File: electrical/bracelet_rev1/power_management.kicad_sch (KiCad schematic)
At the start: 16 parts, among them J1 USB_C_Receptacle_USB2.0_14P, Q1 PMOS, U3 MCP73831T-2ACI/OT, U4 XC6222B331MR-G

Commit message: Many schematic updates
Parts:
- added C25: 120pF, symbol Device:C
- added C26: 22uF, symbol Device:C
- added C27: 4.7uF, symbol Device:C
- added D3: D_Schottky, symbol Device:D_Schottky
- added L5: 1.0uH, symbol Device:L
- added Q2: PMOS, symbol Simulation_SPICE:PMOS
- added R10: 100k, symbol Device:R
- added R11: 499k, symbol Device:R
- added R12: 10k, symbol Device:R
- added R9: 200k, symbol Device:R
- added U6: TPS62A01DRL, Package_TO_SOT_SMD:SOT-563, symbol Regulator_Switching:TPS62A01DRL
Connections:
- net +BATT: now also Q2.1 (D)
- net GND: now also C26.2, C27.2, R10.2, R12.1, U6.1 (GND)
- net USB_VBUS: now also D3.2 (A), Q2.2 (G), R12.2
- net VDD renamed 3V3
- new net: C27.1, D3.1 (K), Q2.3 (S), R11.1, U6.3 (VIN), U6.4 (EN)
- new net: R11.2, U6.6 (PG)
- new net: L5.1, U6.2 (SW)
- new net: C25.2, R10.1, R9.2, U6.5 (FB)
- new net 1V8: C25.1, C26.1, L5.2, R9.1
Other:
- note added: "R1 = R2 x ((Vout/Vfb) - 1) = R2 x ((Vout/0.6V) - 1) => Select R2 as 100k (From datasheet) Sec 8.2"
- moved on the sheet: C16, C17, C18, C19, D1, D2, J1, Q1, R3, R4, R5, R6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

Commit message: Mostly finihsed hopefully but still needs clean up anyway
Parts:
- added J3: Conn_01x02, symbol Connector_Generic:Conn_01x02
- added R16: 200k, symbol Device:R
- added R17: 100k, symbol Device:R
- added R2: 100m, symbol Device:R_Shunt
- added U8: INA180A1, Package_TO_SOT_SMD:SOT-23-5, symbol Amplifier_Current:INA180A1
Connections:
- net +BATT: now also R16.1, R2.4
- net 3V3: now also U8.5 (V+)
- net GND: now also J3.2 (Pin_2), R17.2, U8.2 (GND)
- new net: J3.1 (Pin_1), R2.1
- new net: R2.2, U8.4 (-)
- new net: R2.3, U8.3 (+)
- new net CURR_SENSE: U8.1
- new net VBATT_SENSE: R16.2, R17.1
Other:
- moved on the sheet: C16, C17, C18, C19, C25, C26, C27, D1, D2, D3, J1, L5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

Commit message: May updates
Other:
- note added: "1V8 Buck"
- note added: "3V3 LDO"
- note added: "Battery Charging IC"
- note added: "Battery Current Sensing"
- note added: "Note: Not sure what Cin should be (C19)"
- note added: "USB-C Input"
- note removed: "Note: Maybe add reverse current protection here?"
- note removed: "Note: Not sure what Cin should be"
- moved on the sheet: C16, C17, C18, C19, C25, C26, C27, D1, D2, D3, J3, L5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

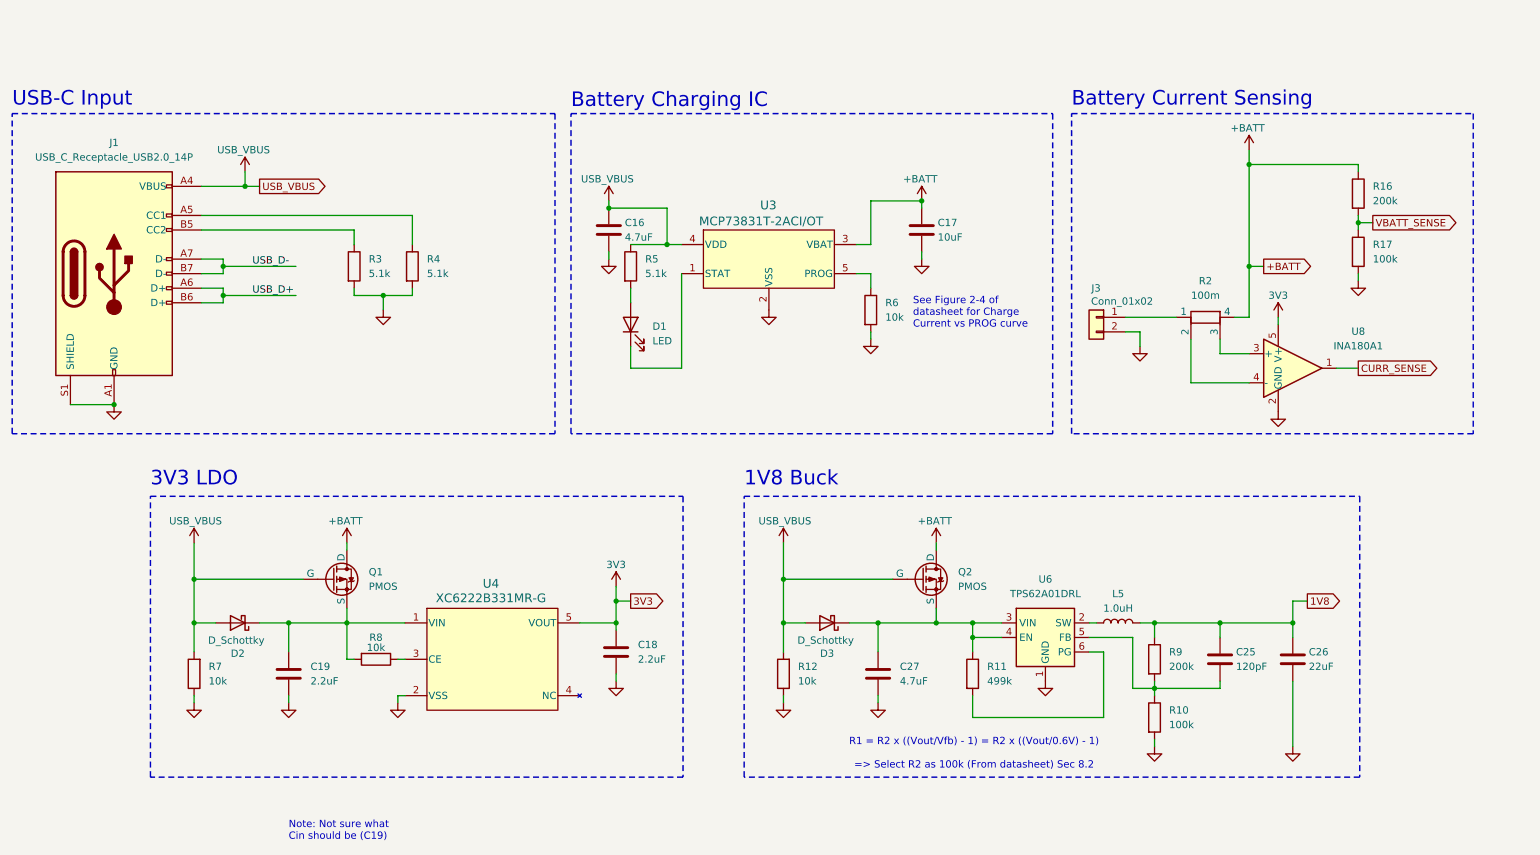
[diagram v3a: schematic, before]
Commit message: Redo component numbers
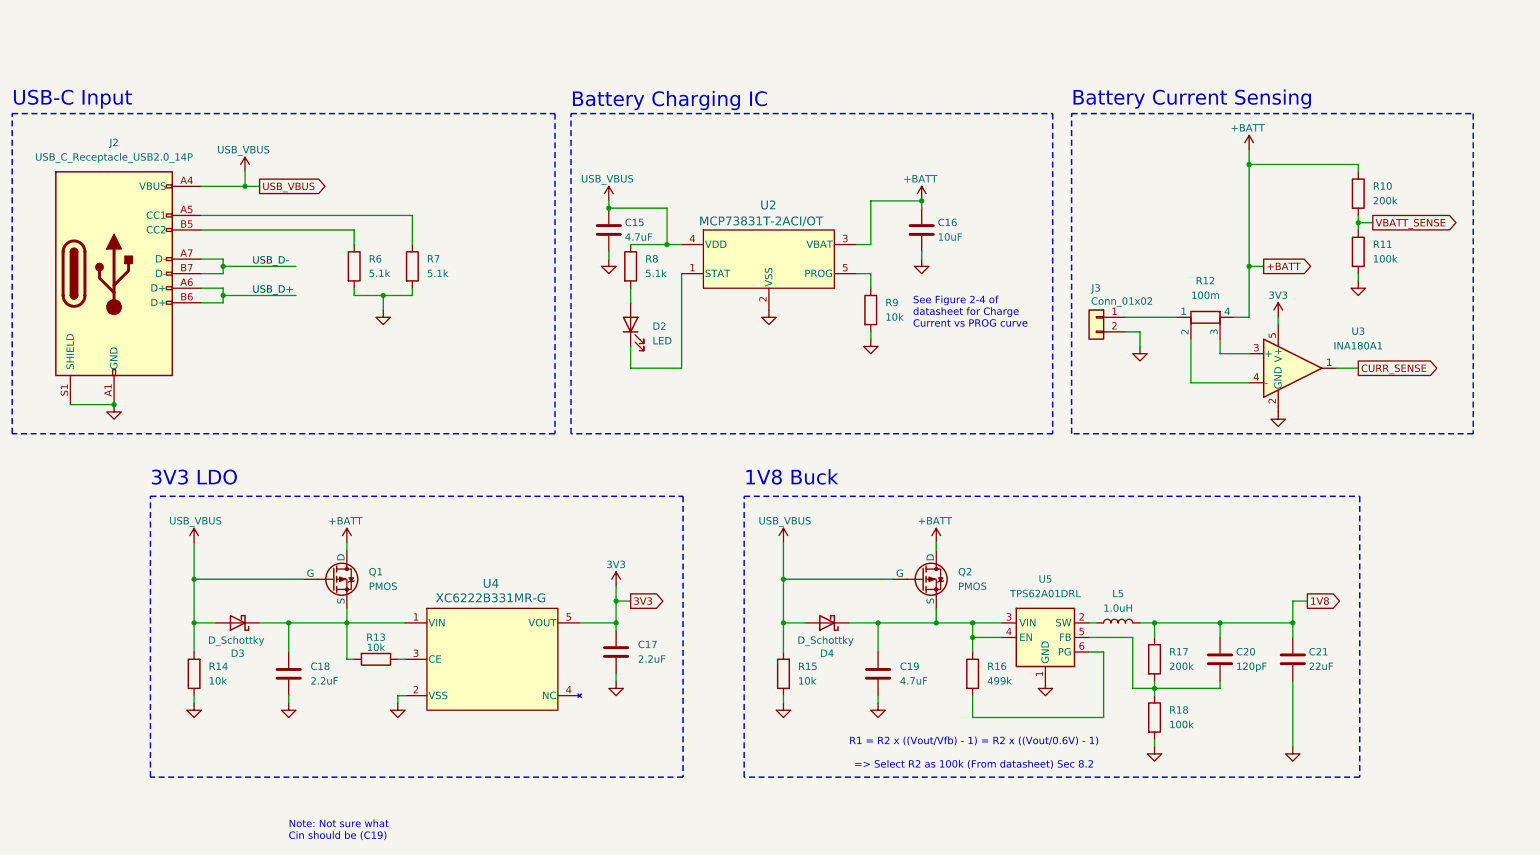
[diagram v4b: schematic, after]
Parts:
- renumbered C16 to C15, C17 to C16, C18 to C17, C19 to C18, C27 to C19, C25 to C20, C26 to C21, D1 to D2, D2 to D3, D3 to D4, J1 to J2, R16 to R10, R17 to R11, R2 to R12, R8 to R13, R7 to R14, R12 to R15, R11 to R16, R9 to R17, R10 to R18, R3 to R6, R4 to R7, R5 to R8, R6 to R9, U3 to U2, U8 to U3, U6 to U5

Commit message: Updated more things
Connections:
- net USB_D+ is gone; now on net GND: J2.A6 (D+), J2.B6 (D+)
- net USB_D- is gone; now on net GND: J2.A7 (D-), J2.B7 (D-)

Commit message: More schematic stuff
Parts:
- C15, C16, C17, C18, C19, C20, C21: footprint (none) -> Capacitor_SMD:C_0603_1608Metric_Pad1.08x0.95mm_HandSolder
- D2: footprint (none) -> LED_SMD:LED_0603_1608Metric_Pad1.05x0.95mm_HandSolder
- D3, D4: footprint (none) -> Diode_SMD:D_0603_1608Metric_Pad1.05x0.95mm_HandSolder
- J3: footprint (none) -> Connector_JST:JST_PH_B2B-PH-K_1x02_P2.00mm_Vertical
- L5: footprint (none) -> Inductor_SMD:L_0603_1608Metric_Pad1.05x0.95mm_HandSolder
- Q1, Q2: footprint (none) -> Package_TO_SOT_SMD:SOT-23-3
- R10, R11, R13, R14, R15, R16, R17, R18, R6, R7, R8, R9: footprint (none) -> Resistor_SMD:R_0603_1608Metric_Pad0.98x0.95mm_HandSolder
- R12: footprint (none) -> Resistor_SMD:R_Shunt_Ohmite_LVK12
- U2: footprint SOT-23-5_MC_MCH -> (none)
- U4: footprint SOT-25_TOR -> (none)
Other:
- note added: "Note: Not sure what Cin should be (C18)"
- note removed: "Note: Not sure what Cin should be (C19)"
